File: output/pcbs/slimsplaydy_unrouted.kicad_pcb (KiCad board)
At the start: 2 copper layers, 256.2 x 89.4 mm, 40 parts

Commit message: Add battery footprint, change outline.
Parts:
- moved MCU1 0.71 mm to (195.2, 103.4)
- moved MCU2 0.71 mm to (240.2, 103.4)
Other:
- board size 256.2 x 89.4 mm -> 254.3 x 87.3 mm

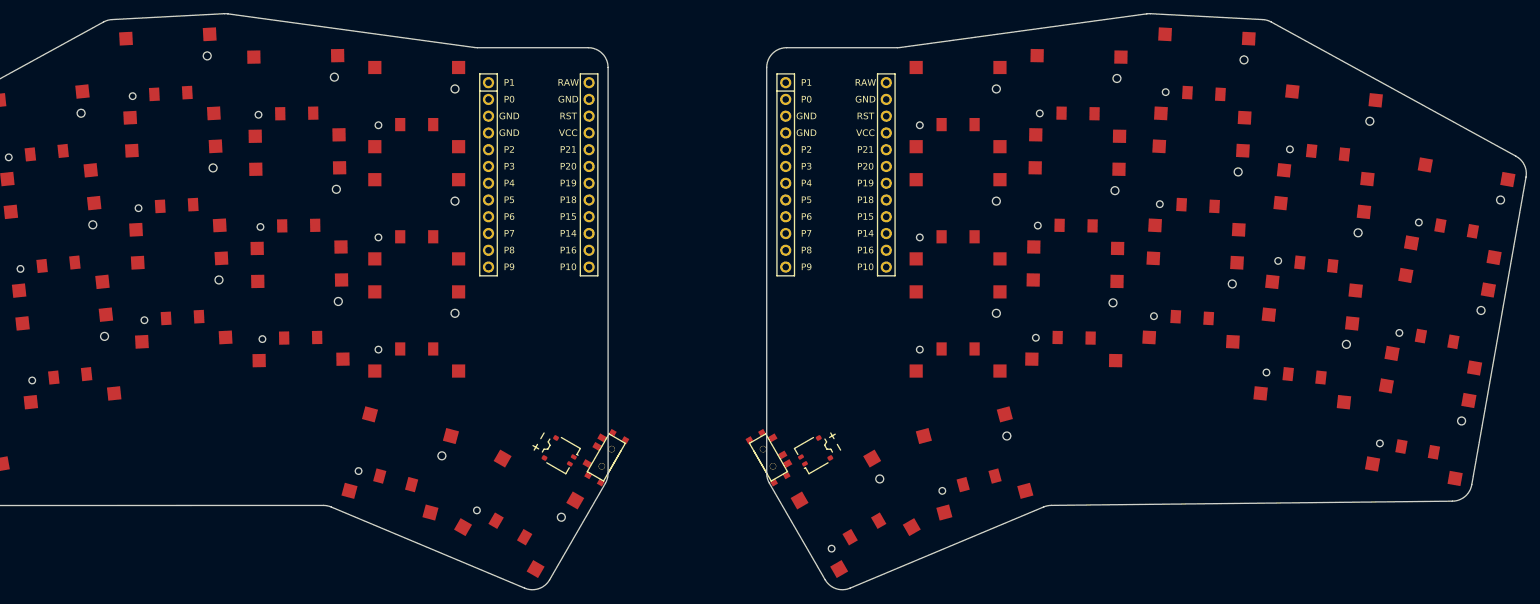
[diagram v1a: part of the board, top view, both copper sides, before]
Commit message: Create first draft design and routing for both sides.
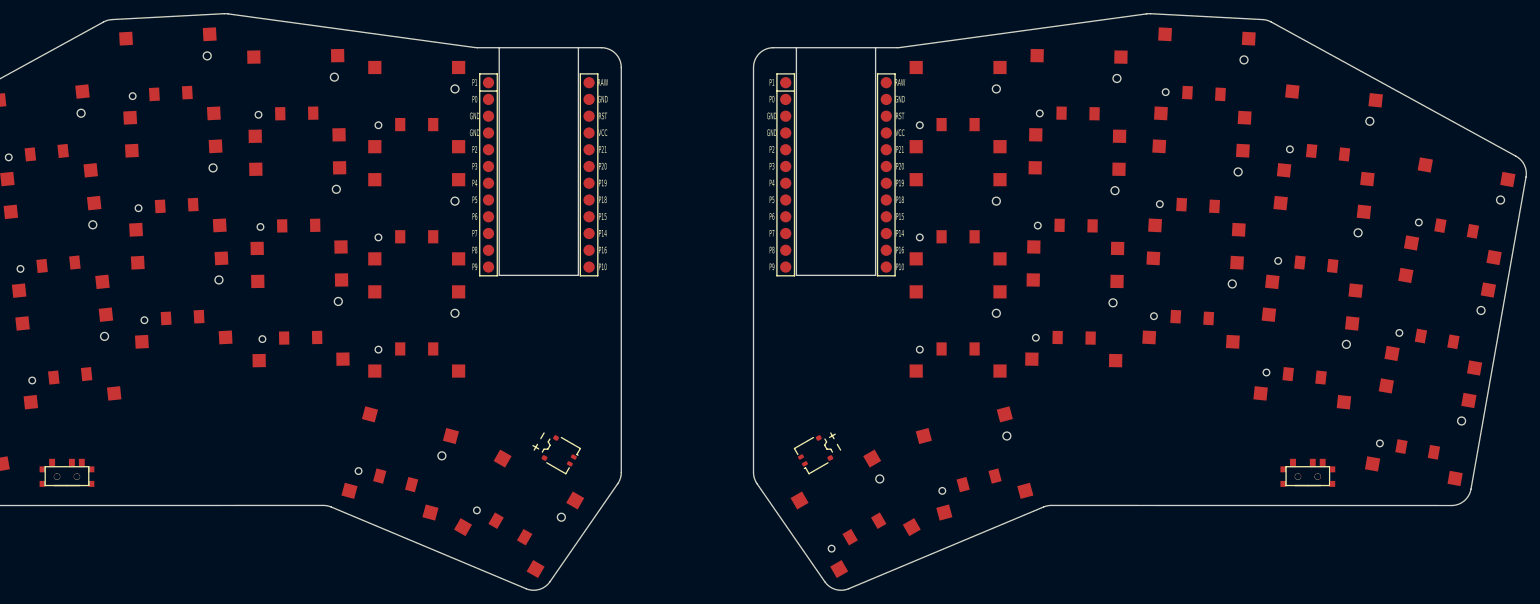
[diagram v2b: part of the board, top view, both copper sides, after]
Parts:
- moved T1 81.8 mm to (123.7, 150.4), turned to 180 degrees
- moved T2 81.8 mm to (311.7, 150.4), turned to -180 degrees
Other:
- board size 254.3 x 87.3 mm -> 254.3 x 87.4 mm

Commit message: Add new reversable PG1316S footprint.
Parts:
- S1, S10, S11, S12, S13, S14, S15, S16, S17, S18, S19, S2, S20, S21, S22, S23, S24, S25, S26, S27, S28, S29, S3, S30, S31, S32, S33, S34, S4, S5, S6, S7, S8, S9: footprint CPG1316S01D02_mikeholscher -> PG1316S

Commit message: Reposition battery/connector, work on mounting holes.
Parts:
- removed T1, T2: , E73:SPDT_C128955
- added PWR1: , ceoloide:power_switch_smd_side, F.Cu at (126.0, 148.2)
- added PWR2: , ceoloide:power_switch_smd_side, F.Cu at (314.0, 148.2)
- moved S20 3.21 mm to (337.4, 108.4), turned to -11 degrees
- moved S9 3.17 mm to (141.6, 87.5)
- moved S7 3.17 mm to (143.4, 121.5)
- moved S8 3.17 mm to (142.5, 104.5)
- moved S11 3.17 mm to (161.0, 107.5)
- moved S10 3.17 mm to (161.3, 124.5)
- moved S4 3.17 mm to (126.2, 130.3)
- moved S5 3.17 mm to (124.4, 113.4)
- moved S23 3.17 mm to (317.3, 96.5)
- moved S12 3.17 mm to (160.7, 90.5)
- moved MCU1 3.17 mm to (197.5, 101.2)
- moved MCU2 3.17 mm to (242.5, 101.2)
- moved S15 3.17 mm to (179.0, 92.2)
- moved S32 3.17 mm to (261.0, 92.2)
- moved S21 3.17 mm to (313.8, 130.3)
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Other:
- board size 254.3 x 87.4 mm -> 259.5 x 94.7 mm

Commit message: Finish up mounting, add case outlines, export step.
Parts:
- removed PWR1, PWR2: , ceoloide:power_switch_smd_side
- added T1: , E73:SPDT_C128955, F.Cu at (123.4, 150.4)
- added T2: , E73:SPDT_C128955, F.Cu at (311.2, 150.4)
- moved MCU2 5.00 mm to (238.9, 104.7), turned to 1 degrees
- moved S32 4.90 mm to (257.2, 95.3), turned to 1 degrees
- moved S29 4.74 mm to (275.4, 93.3), turned to 0 degrees
- moved S31 4.68 mm to (257.5, 112.3), turned to 1 degrees
- moved S26 4.59 mm to (294.5, 90.0), turned to -2 degrees
- moved CONN2 4.51 mm to (236.3, 148.3), turned to 121 degrees
- moved S28 4.50 mm to (275.4, 110.3), turned to 0 degrees
- moved S30 4.46 mm to (257.8, 129.3), turned to 1 degrees
- moved S25 4.35 mm to (293.9, 107.0), turned to -2 degrees
- moved S17 4.33 mm to (191.8, 157.2), turned to -31 degrees
- moved S34 4.33 mm to (242.8, 157.2), turned to 31 degrees
- moved CONN1 4.32 mm to (198.3, 148.3), turned to -121 degrees
- moved S23 4.29 mm to (313.6, 98.6), turned to -5 degrees
- moved S27 4.27 mm to (275.4, 127.3), turned to 0 degrees
- moved S33 4.18 mm to (260.7, 149.3), turned to 16 degrees
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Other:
- board size 259.5 x 94.7 mm -> 253.4 x 88.2 mm
